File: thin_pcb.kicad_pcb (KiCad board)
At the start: 2 copper layers, 95.2 x 95.2 mm, 190 parts, among them J01 Conn_01x02, J02 Conn_01x02, J04 Conn_01x02, J06 Conn_01x02, J07 Conn_01x02, J08 Conn_01x02, J1 USB_B_Micro, J11 Conn_01x03, J12 Conn_01x03, J13 Conn_01x03, J14 Conn_01x03, J15 Conn_01x03, J16 Conn_01x03, J17 Conn_01x03, J18 Conn_01x03, J2 AudioJack4_Ground, J21 Conn_01x07, J22 Conn_01x07, J23 Conn_01x07, J24 Conn_01x07, J25 Conn_01x07, J26 Conn_01x07, J27 Conn_01x07, J28 Conn_01x07, J3 AudioJack4_Ground, J31 Conn_01x07, J32 Conn_01x07, J33 Conn_01x07, J34 Conn_01x07, J35 Conn_01x07, J36 Conn_01x07, J37 Conn_01x07, J38 Conn_01x07, J4 Conn_01x06, J41 Conn_01x04, J42 Conn_01x04, J43 Conn_01x04, J44 Conn_01x04, J45 Conn_01x04, J46 Conn_01x04, J47 Conn_01x04, J48 Conn_01x04, J5 Conn_01x06, J51 Conn_01x01, J52 Conn_01x01, J53 Conn_01x01, J54 Conn_01x01, J55 Conn_01x01, J56 Conn_01x01, J57 Conn_01x01, J58 Conn_01x01, J6 Conn_02x02, J7 Conn_01x02, SW11 SW_Push, SW12 SW_Push, SW13 SW_Push, SW14 SW_Push, SW15 SW_Push, SW21 SW_Push, SW22 SW_Push, SW23 SW_Push, SW24 SW_Push, SW25 SW_Push, SW252 SW_Push, SW31 SW_Push, SW32 SW_Push, SW33 SW_Push, SW34 SW_Push, SW35 SW_Push, SW41 SW_Push, SW42 SW_Push, SW422 SW_Push, SW43 SW_Push, SW44 SW_Push, SW45 SW_Push, SW452 SW_Push, SW51 SW_Push, SW52 SW_Push, SW522 SW_Push, SW53 SW_Push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

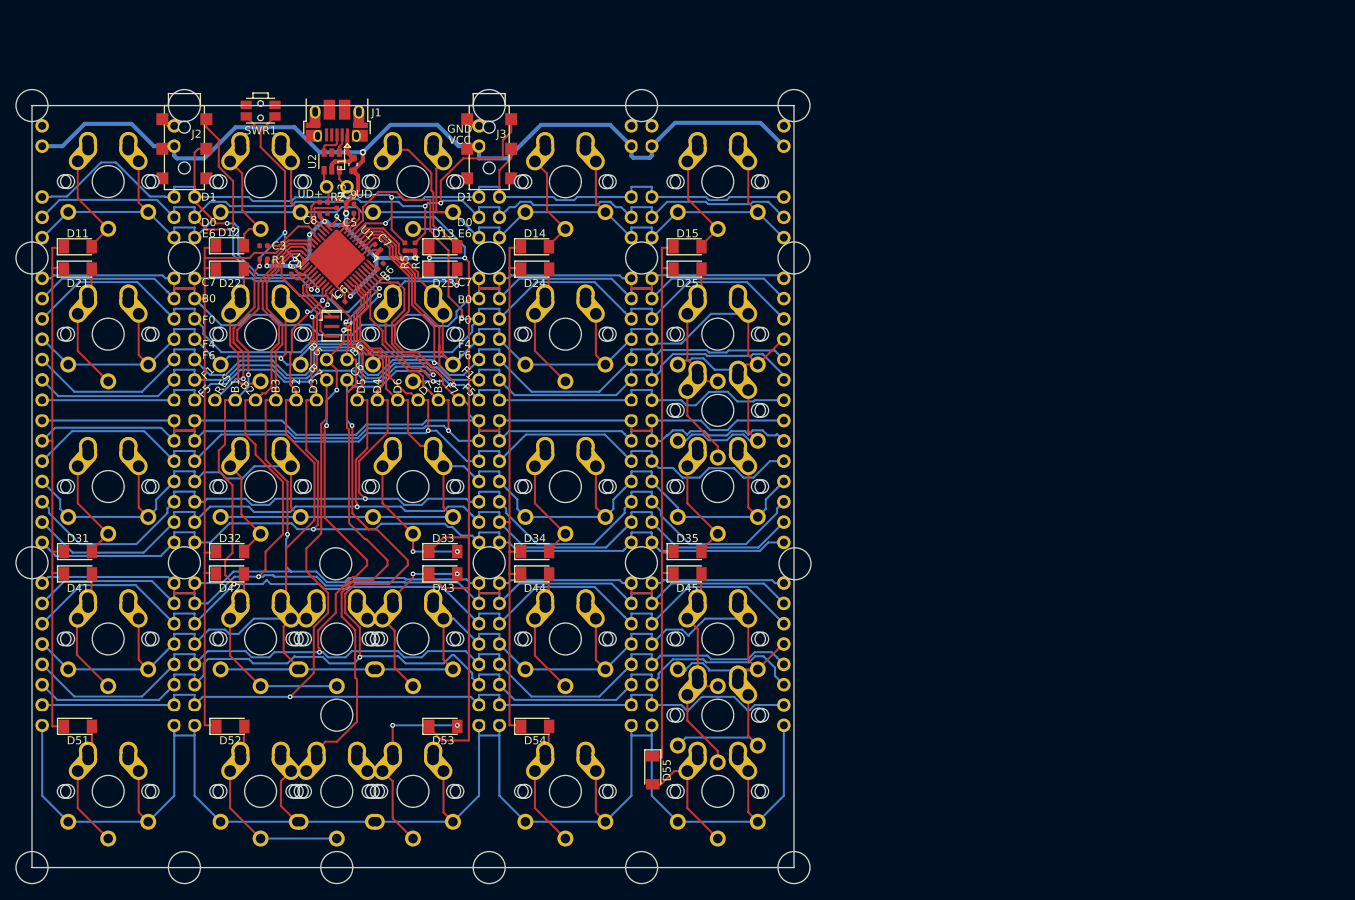
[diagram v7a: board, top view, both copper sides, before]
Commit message: reset switch & aligning
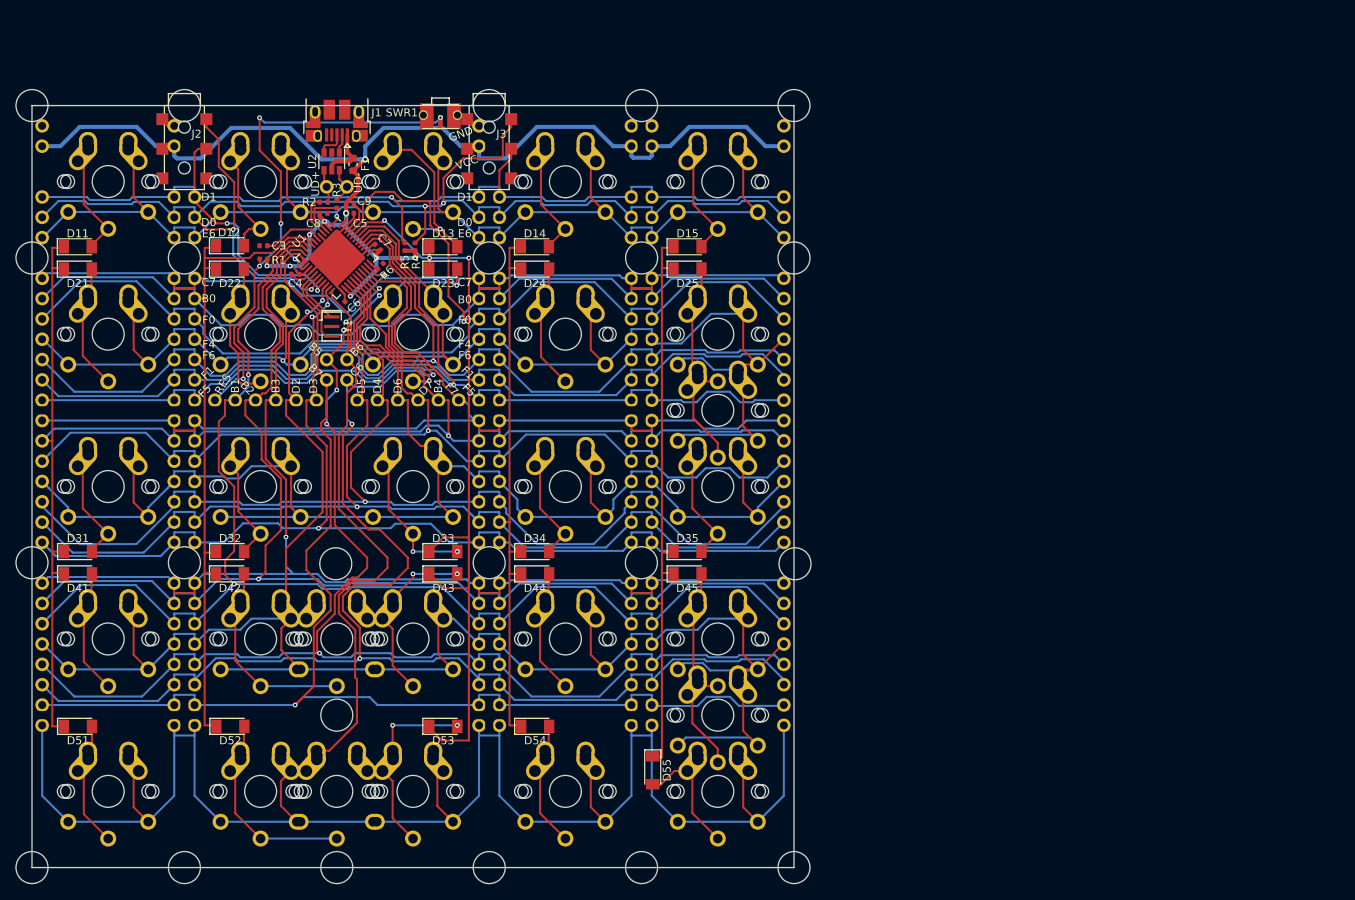
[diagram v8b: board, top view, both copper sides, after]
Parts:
- removed the ? at (105.4, 81.9) (x2)
- added ? (x2): , , F.Cu at (105.4, 81.9)
- SWR1: footprint Button_Switch_SMD:SW_SPST_EVQP7C -> lib:SW_Reset
- moved SWR1 22.5 mm to (102.5, 59.1)
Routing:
- net RESET: track 52.7 -> 70.2 mm, vias 4 -> 6
- net D1: track 149.9 -> 146.5 mm
- net B6: track 286.2 -> 289.1 mm
- net B5: track 170.2 -> 167.9 mm
- net D2: track 236.2 -> 238.4 mm
- net D6: track 189.7 -> 191.6 mm
- net B4: track 200.8 -> 199.3 mm
- net E6: track 149.3 -> 150.8 mm
- net F4: track 195.8 -> 197.3 mm
- net F1: track 222.5 -> 221.5 mm
- net F5: track 135.8 -> 134.8 mm
- net F6: track 140.2 -> 139.2 mm
- net Net-(D23-Pad2): track 25.1 -> 24.3 mm
- net F7: track 136.7 -> 135.9 mm
- net D7: track 138.0 -> 137.3 mm
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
